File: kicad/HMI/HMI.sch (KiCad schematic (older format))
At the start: 54 parts, among them J2 SWD, J3 DEM 128128A TMH-PW-N, J4 RIBBON, SW1 SW_Push, SW10 SW_Push, SW11 SW_Push, SW12 SW_Push, SW13 SW_Push, SW14 SW_Push, SW15 SW_Push, SW16 SW_Push, SW17 SW_Push, SW18 SW_Push, SW19 SW_Push, SW2 SW_Push, SW20 SW_Push, SW3 SW_Push, SW4 SW_Push, SW5 SW_Push, SW6 SW_Push, SW7 SW_Push, SW8 SW_Push, SW9 SW_Push, U1 STM32L011K4Tx, X1 ASV-4.000MHZ-EJ-T

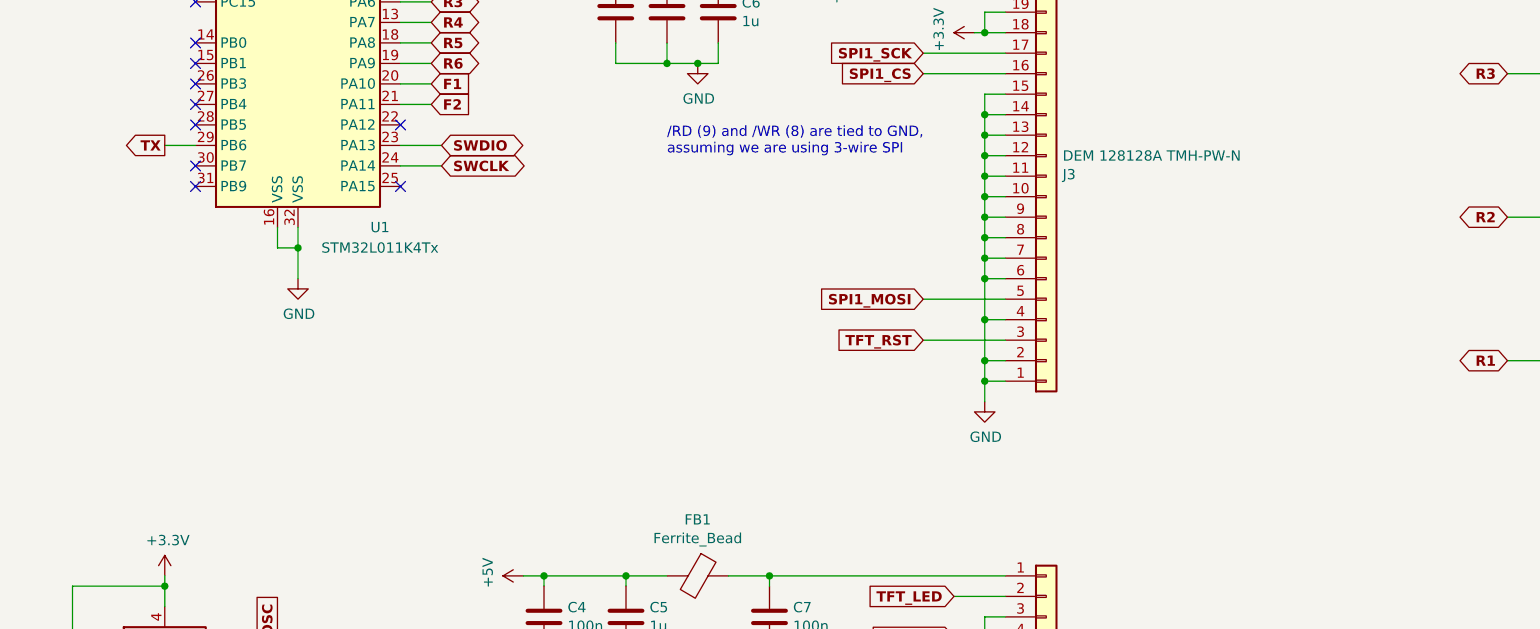
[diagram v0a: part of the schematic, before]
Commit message: Adding mounting holes, U2. Corrected part number for J3.
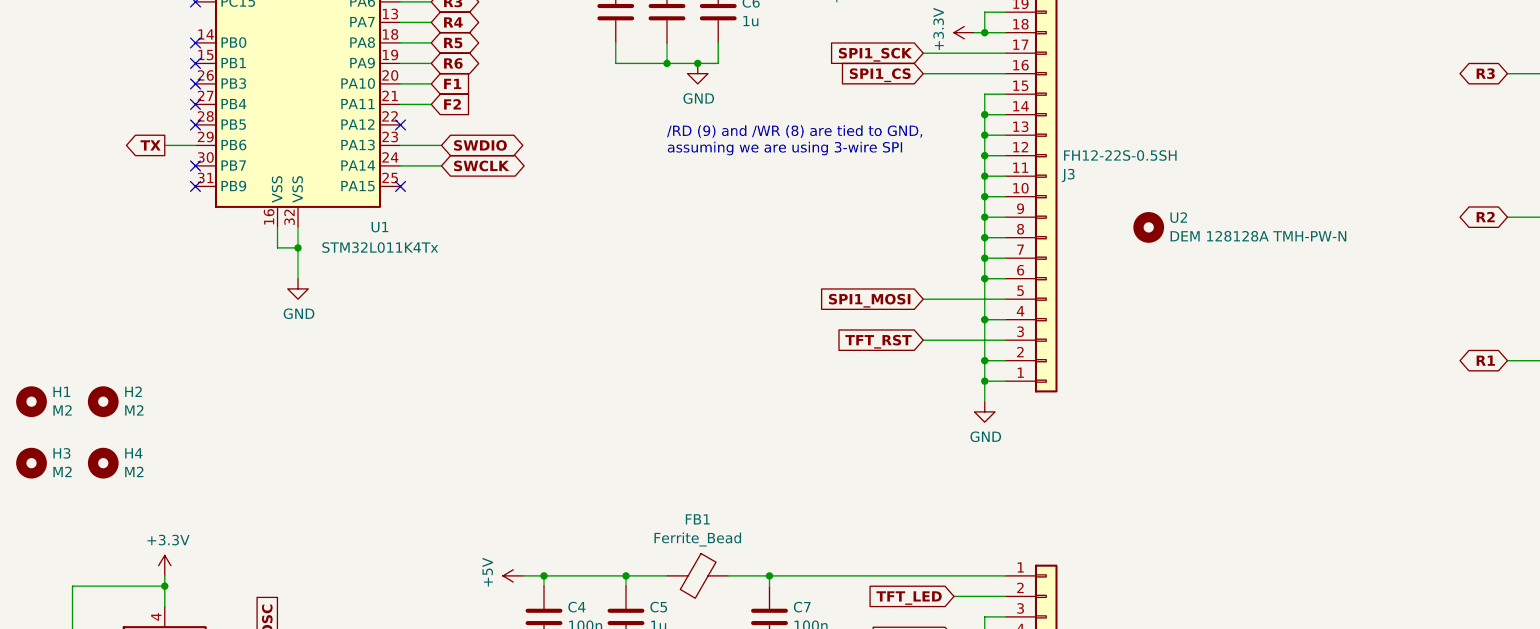
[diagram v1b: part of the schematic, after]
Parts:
- added H1, H2, H3, H4: M2, MountingHole:MountingHole_2.2mm_M2_ISO14580_Pad, symbol Mechanical:MountingHole
- added U2: DEM 128128A TMH-PW-N, HMI:DEM_128128A_TMH-PW-N, symbol Mechanical:MountingHole
- J3: value DEM 128128A TMH-PW-N -> FH12-22S-0.5SH
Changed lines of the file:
@@
 P 5900 4300
 F 0 "J3" H 5980 4292 50  0000 L CNN
-F 1 "DEM 128128A TMH-PW-N" H 5980 4201 50  0000 L CNN
+F 1 "FH12-22S-0.5SH" H 5980 4201 50  0000 L CNN
 F 2 "Connector_FFC-FPC:Hirose_FH12-22S-0.5SH_1x22-1MP_P0.50mm_Horizontal" H 5900 4300 50  0001 C CNN
 F 3 "~" H 5900 4300 50  0001 C CNN
@@
 	3800 3750 4050 3750
 Connection ~ 4050 3750
+$Comp
+L Mechanical:MountingHole U2
+U 1 1 5FB8FAE3
+P 6400 4550
+F 0 "U2" H 6500 4596 50  0000 L CNN
+F 1 "DEM 128128A TMH-PW-N" H 6500 4505 50  0000 L CNN
+F 2 "HMI:DEM_128128A_TMH-PW-N" H 6400 4550 50  0001 C CNN
+F 3 "~" H 6400 4550 50  0001 C CNN
+	1    6400 4550
+	1    0    0    -1
+$EndComp
+$Comp
+L Mechanical:MountingHole H1
+U 1 1 5FB9CD26
+P 950 5400
+F 0 "H1" H 1050 5446 50  0000 L CNN
+F 1 "M2" H 1050 5355 50  0000 L CNN
+F 2 "MountingHole:MountingHole_2.2mm_M2_ISO14580_Pad" H 950 5400 50  0001 C CNN
+F 3 "~" H 950 5400 50  0001 C CNN
+	1    950  5400
+	1    0    0    -1
+$EndComp
+$Comp
+L Mechanical:MountingHole H2
+U 1 1 5FB9F230
+P 1300 5400
+F 0 "H2" H 1400 5446 50  0000 L CNN
+F 1 "M2" H 1400 5355 50  0000 L CNN
+F 2 "MountingHole:MountingHole_2.2mm_M2_ISO14580_Pad" H 1300 5400 50  0001 C CNN
+F 3 "~" H 1300 5400 50  0001 C CNN
+	1    1300 5400
+	1    0    0    -1
+$EndComp
+$Comp
+L Mechanical:MountingHole H3
+U 1 1 5FB9F543
+P 950 5700
+F 0 "H3" H 1050 5746 50  0000 L CNN
+F 1 "M2" H 1050 5655 50  0000 L CNN
+F 2 "MountingHole:MountingHole_2.2mm_M2_ISO14580_Pad" H 950 5700 50  0001 C CNN
+F 3 "~" H 950 5700 50  0001 C CNN
+	1    950  5700
+	1    0    0    -1
+$EndComp
+$Comp
+L Mechanical:MountingHole H4
+U 1 1 5FB9F863
+P 1300 5700
+F 0 "H4" H 1400 5746 50  0000 L CNN
+F 1 "M2" H 1400 5655 50  0000 L CNN
+F 2 "MountingHole:MountingHole_2.2mm_M2_ISO14580_Pad" H 1300 5700 50  0001 C CNN
+F 3 "~" H 1300 5700 50  0001 C CNN
+	1    1300 5700
+	1    0    0    -1
+$EndComp
 $EndSCHEMATC

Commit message: Update
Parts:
- SW1, SW14: footprint Button_Switch_THT:SW_Tactile_SKHH_Angled -> Button_Switch_SMD:SW_Push_1P1T_NO_CK_KMR2
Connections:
- net F1: now also SW1.1; no longer SW1.2
- net F2: now also SW14.1; no longer SW14.2
- net GND: now also SW1.2, SW14.2, U1.31 (PB9); no longer SW1.1, SW14.1
- no-connect marks 11 -> 10
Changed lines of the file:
@@
 R6
 NoConn ~ 1750 4250
-NoConn ~ 1750 4350
 NoConn ~ 1750 3650
 NoConn ~ 1750 3750
@@
 Connection ~ 6850 1550
 $Comp
-L Switch:SW_Push SW1
-U 1 1 5E314A54
-P 8650 1200
-F 0 "SW1" V 8604 1348 50  0000 L CNN
-F 1 "SW_Push" V 8695 1348 50  0000 L CNN
-F 2 "Button_Switch_THT:SW_Tactile_SKHH_Angled" H 8650 1400 50  0001 C CNN
-F 3 "~" H 8650 1400 50  0001 C CNN
-	1    8650 1200
-	-1   0    0    -1
-$EndComp
-$Comp
-L Switch:SW_Push SW14
-U 1 1 5E315963
-P 9700 1200
-F 0 "SW14" V 9654 1348 50  0000 L CNN
-F 1 "SW_Push" V 9745 1348 50  0000 L CNN
-F 2 "Button_Switch_THT:SW_Tactile_SKHH_Angled" H 9700 1400 50  0001 C CNN
-F 3 "~" H 9700 1400 50  0001 C CNN
-	1    9700 1200
-	-1   0    0    -1
-$EndComp
-$Comp
 L power:GND #PWR023
 U 1 1 5E315D15
@@
 	1    0    0    -1
 $EndComp
+$Comp
+L Switch:SW_Push SW14
+U 1 1 61181ECB
+P 9700 1200
+F 0 "SW14" V 9654 1348 50  0000 L CNN
+F 1 "SW_Push" V 9745 1348 50  0000 L CNN
+F 2 "Button_Switch_SMD:SW_Push_1P1T_NO_CK_KMR2" H 9700 1400 50  0001 C CNN
+F 3 "~" H 9700 1400 50  0001 C CNN
+	1    9700 1200
+	1    0    0    -1
+$EndComp
+$Comp
+L Switch:SW_Push SW1
+U 1 1 611AF5F3
+P 8650 1200
+F 0 "SW1" V 8604 1348 50  0000 L CNN
+F 1 "SW_Push" V 8695 1348 50  0000 L CNN
+F 2 "Button_Switch_SMD:SW_Push_1P1T_NO_CK_KMR2" H 8650 1400 50  0001 C CNN
+F 3 "~" H 8650 1400 50  0001 C CNN
+	1    8650 1200
+	1    0    0    -1
+$EndComp
+Wire Wire Line
+	1750 4350 1750 4650
+Wire Wire Line
+	1750 4650 2150 4650
+Connection ~ 2150 4650
 $EndSCHEMATC
